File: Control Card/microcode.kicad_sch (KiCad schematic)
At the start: 19 parts, among them U1 CY7C1021D, U100 74LS08, U101 74ACT32, U11 74ACT151, U12 74ACT86, U13 74ACT32, U14 74ACT04, U15 74ACT153, U16 74ACT153, U17 74ACT153, U18 74ACT153, U2 CY7C1021D, U20 74ACT02, U21 74ACT20, U24 74ACT30, U3 CY7C1021D, U44 74ACT11, U53 74ACT04, U61 74ACT32

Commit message: add buffers for the write to the µCODE stuff
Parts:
- removed U100: 74LS08, Package_SO:SOIC-14_3.9x8.7mm_P1.27mm, symbol 74xx:74LS08
- removed U101: 74ACT32, Package_SO:SOIC-14_3.9x8.7mm_P1.27mm, symbol 74xx:74LS32
- added U100: 74LVC1G08, Package_TO_SOT_SMD:SOT-23-5, symbol 74xGxx:74LVC1G08
- added U101: 74LVC1G32, Package_TO_SOT_SMD:SOT-23-5, symbol 74xGxx:74LVC1G32
- added U102: 74LVC1G157, Package_SO:SSOP-8_2.95x2.8mm_P0.65mm, symbol 74xGxx:74LVC2G157
- added U110: 74ACT244, Package_SO:SOIC-20W_7.5x12.8mm_P1.27mm, symbol 74xx:74LS244
- added U111, U112, U113: 74ACT374, Package_SO:SOIC-20W_7.5x12.8mm_P1.27mm, symbol 74xx:74LS374
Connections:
- net GND: now also U100.3 (GND), U101.3 (GND), U102.4 (GND), U102.7 (~G), U110.1 (OEa), U110.10 (GND), U110.19 (OEb), U111.10 (GND), U112.10 (GND), U113.10 (GND)
- net NEXT_0: now also U100.1
- net SUPERVISOR: now also U102.1 (A); no longer U1.27 (A8), U2.27 (A8), U3.27 (A8)
- net VCC: now also U100.5 (VCC), U101.5 (VCC), U102.8 (VCC), U110.20 (VCC), U111.20 (VCC), U112.20 (VCC), U113.20 (VCC)
- net ~FAULT_PENDING~: now also U101.2
- net µCODE_ADDR_SEL_B: now also U101.4
- net µCODE_PAGE0: now also U112.19 (O7), U113.19 (O7)
- net µCODE_PAGE1: now also U112.16 (O6), U113.16 (O6)
- net µCODE_PAGE2: now also U112.15 (O5), U113.15 (O5)
- net µCODE_PAGE3: now also U112.12 (O4), U113.12 (O4)
- net µCODE_PAGE4: now also U112.9 (O3), U113.9 (O3)
- net µCODE_PAGE5: now also U112.6 (O2), U113.6 (O2)
- net µCODE_PAGE6: now also U112.5 (O1), U113.5 (O1)
- net µCODE_WR_ADDR0 renamed µCODE_RW_ADDR0
- net µCODE_RW_ADDR0: now also U111.19 (O7)
- net µCODE_WR_ADDR1 renamed µCODE_RW_ADDR1
- net µCODE_RW_ADDR1: now also U111.16 (O6)
- net µCODE_WR_ADDR2 renamed µCODE_RW_ADDR2
- net µCODE_RW_ADDR2: now also U111.15 (O5)
- net µCODE_WR_ADDR3 renamed µCODE_RW_ADDR3
- net µCODE_RW_ADDR3: now also U111.12 (O4)
- net µCODE_WR_ADDR4 renamed µCODE_RW_ADDR4
- net µCODE_RW_ADDR4: now also U111.9 (O3)
- net µCODE_WR_ADDR5 renamed µCODE_RW_ADDR5
- net µCODE_RW_ADDR5: now also U111.6 (O2)
- net µCODE_WR_ADDR6 renamed µCODE_RW_ADDR6
- net µCODE_RW_ADDR6: now also U111.5 (O1)
- net µCODE_WR_ADDR7 renamed µCODE_RW_ADDR7
- net µCODE_RW_ADDR7: now also U111.2 (O0)
- new net: U100.4, U101.1
- new net DBUS0: U110.17 (I3b)
- new net DBUS1: U110.15 (I2b)
- new net DBUS2: U110.13 (I1b)
- new net DBUS3: U110.11 (I0b)
- new net DBUS4: U110.8 (I3a)
- new net DBUS5: U110.6 (I2a)
- new net DBUS6: U110.4 (I1a)
- new net DBUS7: U110.2 (I0a)
- new net RW_µCODE: U102.6 (~A~/B)
- new net i_DBUS0: U110.3 (O3b), U111.18 (D7), U112.18 (D7), U113.18 (D7)
- new net i_DBUS1: U110.5 (O2b), U111.17 (D6), U112.17 (D6), U113.17 (D6)
- new net i_DBUS2: U110.7 (O1b), U111.14 (D5), U112.14 (D5), U113.14 (D5)
- new net i_DBUS3: U110.9 (O0b), U111.13 (D4), U112.13 (D4), U113.13 (D4)
- new net i_DBUS4: U110.12 (O3a), U111.8 (D3), U112.8 (D3), U113.8 (D3)
- new net i_DBUS5: U110.14 (O2a), U111.7 (D2), U112.7 (D2), U113.7 (D2)
- new net i_DBUS6: U110.16 (O1a), U111.4 (D1), U112.4 (D1), U113.4 (D1)
- new net i_DBUS7: U110.18 (O0a), U111.3 (D0), U112.3 (D0), U113.3 (D0)
- new net ~RW_µCODE~: U100.2
- new net µCODE_RW_SUP: U102.2 (B), U112.2 (O0)
- new net µCODE_SUP: U1.27 (A8), U102.5 (Y), U2.27 (A8), U3.27 (A8)
- no-connect marks 1 -> 2
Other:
- note added: "As currently stands: ~NEXT_0~ ~FAULT_PENDING~ output 0 0 0 (ENCODERx) 1 0 1 (IRx) 0 1 2 (ENCODERx) 1 1 3 (NEXTx) we want: ~RW_µCODE~ ~FAULT_PENDING~ ~NEXT_0~ A B output 0 0 0 0 0 0 (WR_µCODE_R) 0 0 1 1 0 1 (IRx) 0 1 0 0 1 2 (ENCODERx) 0 1 1 1 1 3 (NEXTx) 1 0 0 0 1 2 (ENCODERx) 1 0 1 1 0 1 (IRx) 1 1 0 0 1 2 (ENCODERx) 1 1 1 1 1 3 (NEXTx) B = ~FAULT_PENDING~ or ( ~RW_µCODE~ and NEXT_0 )"
- note added: "Buffer"
- note added: "Execute"
- note added: "Read/Write"
- note added: "Selects supervisor bit between the faults generator and the µCODE_RW registers"
- note removed: "As currently stands: ~NEXT_0~ ~FAULT_PENDING~ output 0 0 0 (ENCODERx) 1 0 1 (IRx) 0 1 2 (ENCODERx) 1 1 3 (NEXTx) we want: ~WR_µCODE~ ~FAULT_PENDING~ ~NEXT_0~ A B output 0 0 0 0 0 0 (WR_µCODE_R) 0 0 1 1 0 1 (IRx) 0 1 0 0 1 2 (ENCODERx) 0 1 1 1 1 3 (NEXTx) 1 0 0 0 1 2 (ENCODERx) 1 0 1 1 0 1 (IRx) 1 1 0 0 1 2 (ENCODERx) 1 1 1 1 1 3 (NEXTx) B = ~FAULT_PENDING~ or ( ~WR_µCODE~ and NEXT_0 )"

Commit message: add the µcode output registers
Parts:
- added U10, U5, U6, U7, U8, U9: 74ACT273, Package_SO:SOIC-20W_7.5x12.8mm_P1.27mm, symbol 74xx:74LS273
- U102: value 74LVC1G157 -> 74LVC2G157
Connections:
- net ALUOP0: now also U10.6 (Q2); no longer U3.31 (D10)
- net ALUOP1: now also U10.5 (Q1); no longer U3.30 (D9)
- net ALUOP_SZ: now also U10.2 (Q0); no longer U3.29 (D8)
- net CODE_PTB: now also U10.19 (Q7); no longer U3.38 (D15)
- net EL0: now also U9.9 (Q3); no longer U3.10 (D3)
- net EL1: now also U9.6 (Q2); no longer U3.9 (D2)
- net EL2: now also U9.5 (Q1); no longer U3.8 (D1)
- net EL3: now also U9.2 (Q0); no longer U3.7 (D0)
- net ER0: now also U9.15 (Q5); no longer U3.14 (D5)
- net ER1: now also U9.12 (Q4); no longer U3.13 (D4)
- net E_MDR_HI: now also U8.2 (Q0); no longer U2.29 (D8)
- net E_MDR_LO: now also U7.19 (Q7); no longer U2.16 (D7)
- net GND: now also U10.10 (GND), U5.10 (GND), U6.10 (GND), U7.10 (GND), U8.10 (GND), U9.10 (GND)
- net LATCH0: now also U7.9 (Q3); no longer U2.10 (D3)
- net LATCH1: now also U7.6 (Q2); no longer U2.9 (D2)
- net LATCH2: now also U7.5 (Q1); no longer U2.8 (D1)
- net LATCH3: now also U7.2 (Q0); no longer U2.7 (D0)
- net LATCH_SZ: now also U10.12 (Q4); no longer U3.35 (D12)
- net MISC0: now also U8.19 (Q7); no longer U2.38 (D15)
- net MISC1: now also U8.16 (Q6); no longer U2.37 (D14)
- net MISC2: now also U8.15 (Q5); no longer U2.36 (D13)
- net MISC3: now also U8.12 (Q4); no longer U2.35 (D12)
- net NEGATE_BR: now also U10.15 (Q5); no longer U3.36 (D13)
- net NEXT0: now also U6.19 (Q7); no longer U1.16 (D7)
- net NEXT1: now also U6.16 (Q6); no longer U1.15 (D6)
- net NEXT2: now also U6.15 (Q5); no longer U1.14 (D5)
- net NEXT3: now also U6.12 (Q4); no longer U1.13 (D4)
- net NEXT4: now also U6.9 (Q3); no longer U1.10 (D3)
- net NEXT5: now also U6.6 (Q2); no longer U1.9 (D2)
- net NEXT6: now also U6.5 (Q1); no longer U1.8 (D1)
- net NEXT7: now also U6.2 (Q0); no longer U1.7 (D0)
- net PRIV: now also U8.5 (Q1); no longer U2.30 (D9)
- net RIMMVAL0: now also U9.19 (Q7); no longer U3.16 (D7)
- net RIMMVAL1: now also U9.16 (Q6); no longer U3.15 (D6)
- net RUSER_PTB: now also U10.16 (Q6); no longer U3.37 (D14)
- net USE_CARRY: now also U10.9 (Q3); no longer U3.32 (D11)
- net VCC: now also U10.20 (VCC), U5.20 (VCC), U6.20 (VCC), U7.20 (VCC), U8.20 (VCC), U9.20 (VCC)
- net XL_MAR: now also U7.12 (Q4); no longer U2.13 (D4)
- net XL_MDR_HI: now also U7.16 (Q6); no longer U2.15 (D6)
- net XL_MDR_LO: now also U7.15 (Q5); no longer U2.14 (D5)
- net XL_MODE: now also U8.6 (Q2); no longer U2.31 (D10)
- net XL_PAGING: now also U8.9 (Q3); no longer U2.32 (D11)
- new net CLKM: U10.11 (Cp), U5.11 (Cp), U6.11 (Cp), U7.11 (Cp), U8.11 (Cp), U9.11 (Cp)
- new net _RESET: U10.1 (~Mr), U5.1 (~Mr), U6.1 (~Mr), U7.1 (~Mr), U8.1 (~Mr), U9.1 (~Mr)
- new net io_ALUOP0: U10.7 (D2), U3.31 (D10)
- new net io_ALUOP1: U10.4 (D1), U3.30 (D9)
- new net io_ALUOP_SZ: U10.3 (D0), U3.29 (D8)
- new net io_CODE_PTB: U10.18 (D7), U3.38 (D15)
- new net io_EL0: U3.10 (D3), U9.8 (D3)
- new net io_EL1: U3.9 (D2), U9.7 (D2)
- new net io_EL2: U3.8 (D1), U9.4 (D1)
- new net io_EL3: U3.7 (D0), U9.3 (D0)
- new net io_ER0: U3.14 (D5), U9.14 (D5)
- new net io_ER1: U3.13 (D4), U9.13 (D4)
- new net io_E_MDR_HI: U2.29 (D8), U8.3 (D0)
- new net io_E_MDR_LO: U2.16 (D7), U7.18 (D7)
- new net io_LATCH0: U2.10 (D3), U7.8 (D3)
- new net io_LATCH1: U2.9 (D2), U7.7 (D2)
- new net io_LATCH2: U2.8 (D1), U7.4 (D1)
- new net io_LATCH3: U2.7 (D0), U7.3 (D0)
- new net io_LATCH_SZ: U10.13 (D4), U3.35 (D12)
- new net io_MISC0: U2.38 (D15), U8.18 (D7)
- new net io_MISC1: U2.37 (D14), U8.17 (D6)
- new net io_MISC2: U2.36 (D13), U8.14 (D5)
- new net io_MISC3: U2.35 (D12), U8.13 (D4)
- new net io_NEGATE_BR: U10.14 (D5), U3.36 (D13)
- new net io_NEXT0: U1.16 (D7), U6.18 (D7)
- new net io_NEXT1: U1.15 (D6), U6.17 (D6)
- new net io_NEXT2: U1.14 (D5), U6.14 (D5)
- new net io_NEXT3: U1.13 (D4), U6.13 (D4)
- new net io_NEXT4: U1.10 (D3), U6.8 (D3)
- new net io_NEXT5: U1.9 (D2), U6.7 (D2)
- new net io_NEXT6: U1.8 (D1), U6.4 (D1)
- new net io_NEXT7: U1.7 (D0), U6.3 (D0)
- new net io_PRIV: U2.30 (D9), U8.4 (D1)
- new net io_RIMMVAL0: U3.16 (D7), U9.18 (D7)
- new net io_RIMMVAL1: U3.15 (D6), U9.17 (D6)
- new net io_RUSER_PTB: U10.17 (D6), U3.37 (D14)
- new net io_USE_CARRY: U10.8 (D3), U3.32 (D11)
- new net io_XL_MAR: U2.13 (D4), U7.13 (D4)
- new net io_XL_MDR_HI: U2.15 (D6), U7.17 (D6)
- new net io_XL_MDR_LO: U2.14 (D5), U7.14 (D5)
- new net io_XL_MODE: U2.31 (D10), U8.7 (D2)
- new net io_XL_PAGING: U2.32 (D11), U8.8 (D3)

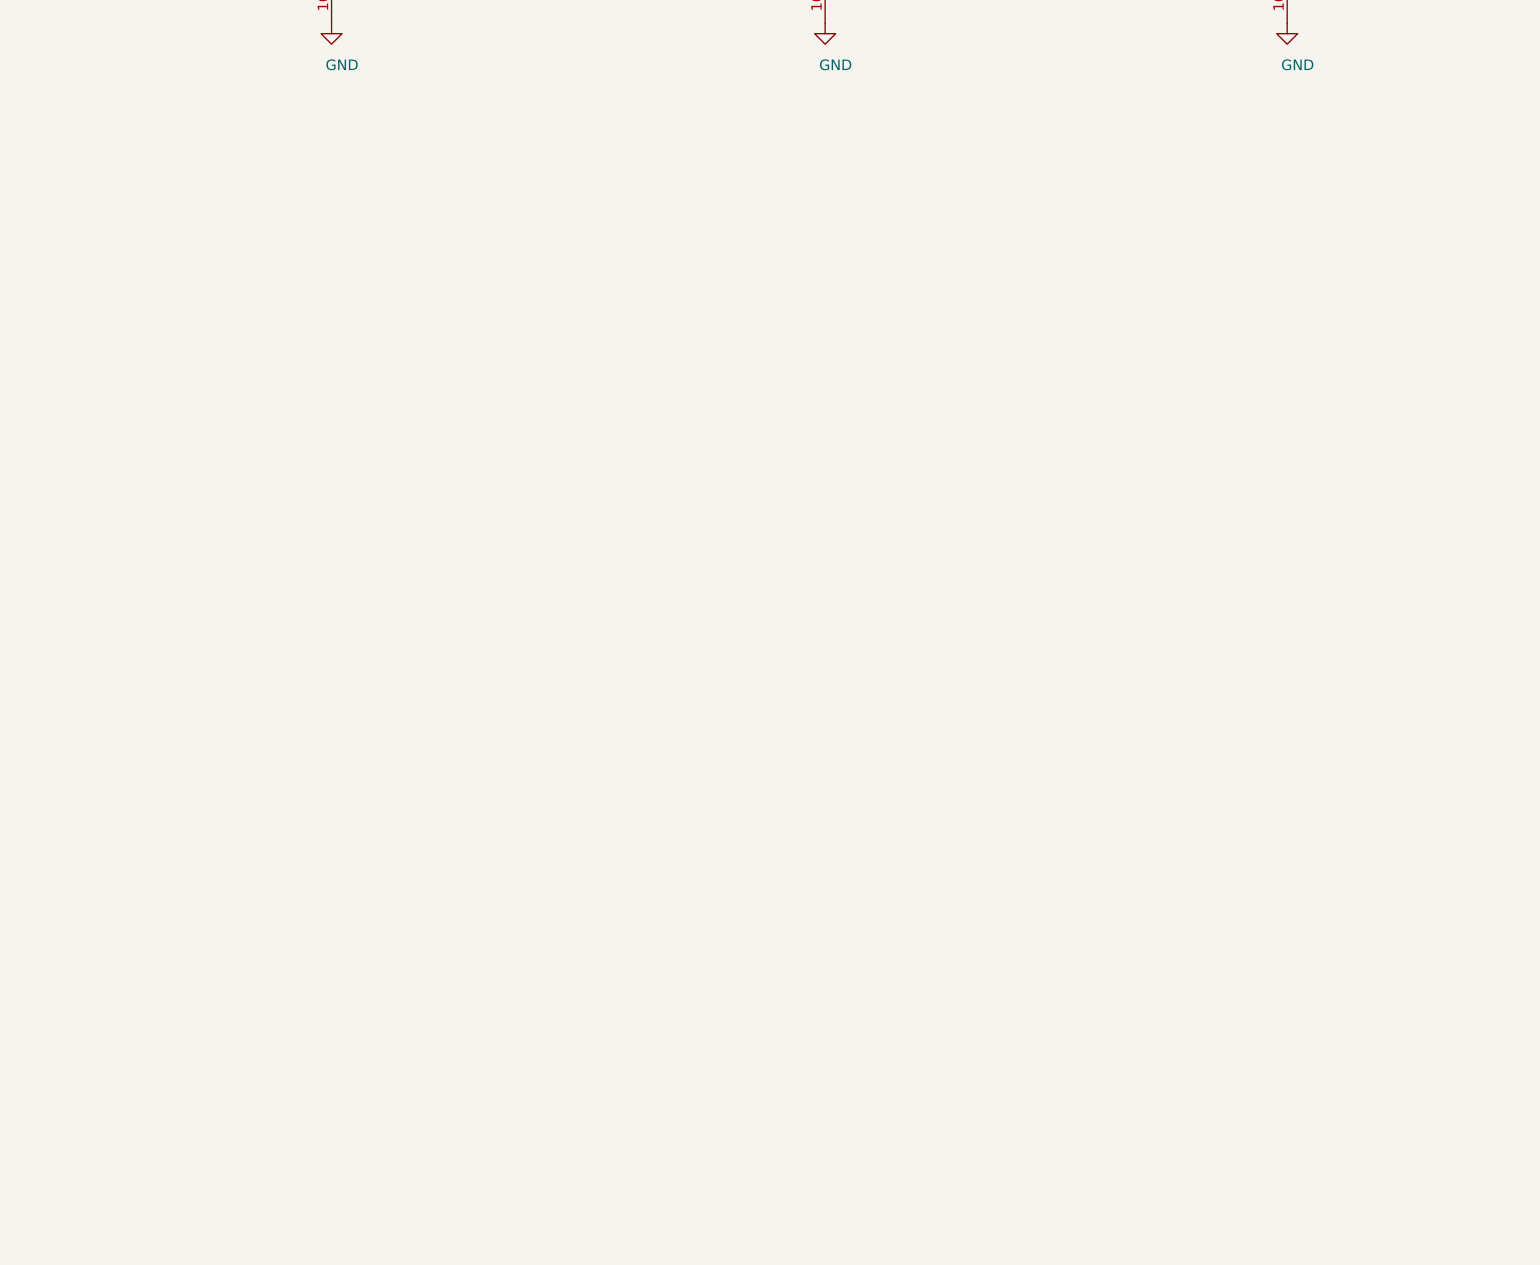
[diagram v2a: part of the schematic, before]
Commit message: add the µcode data write registers
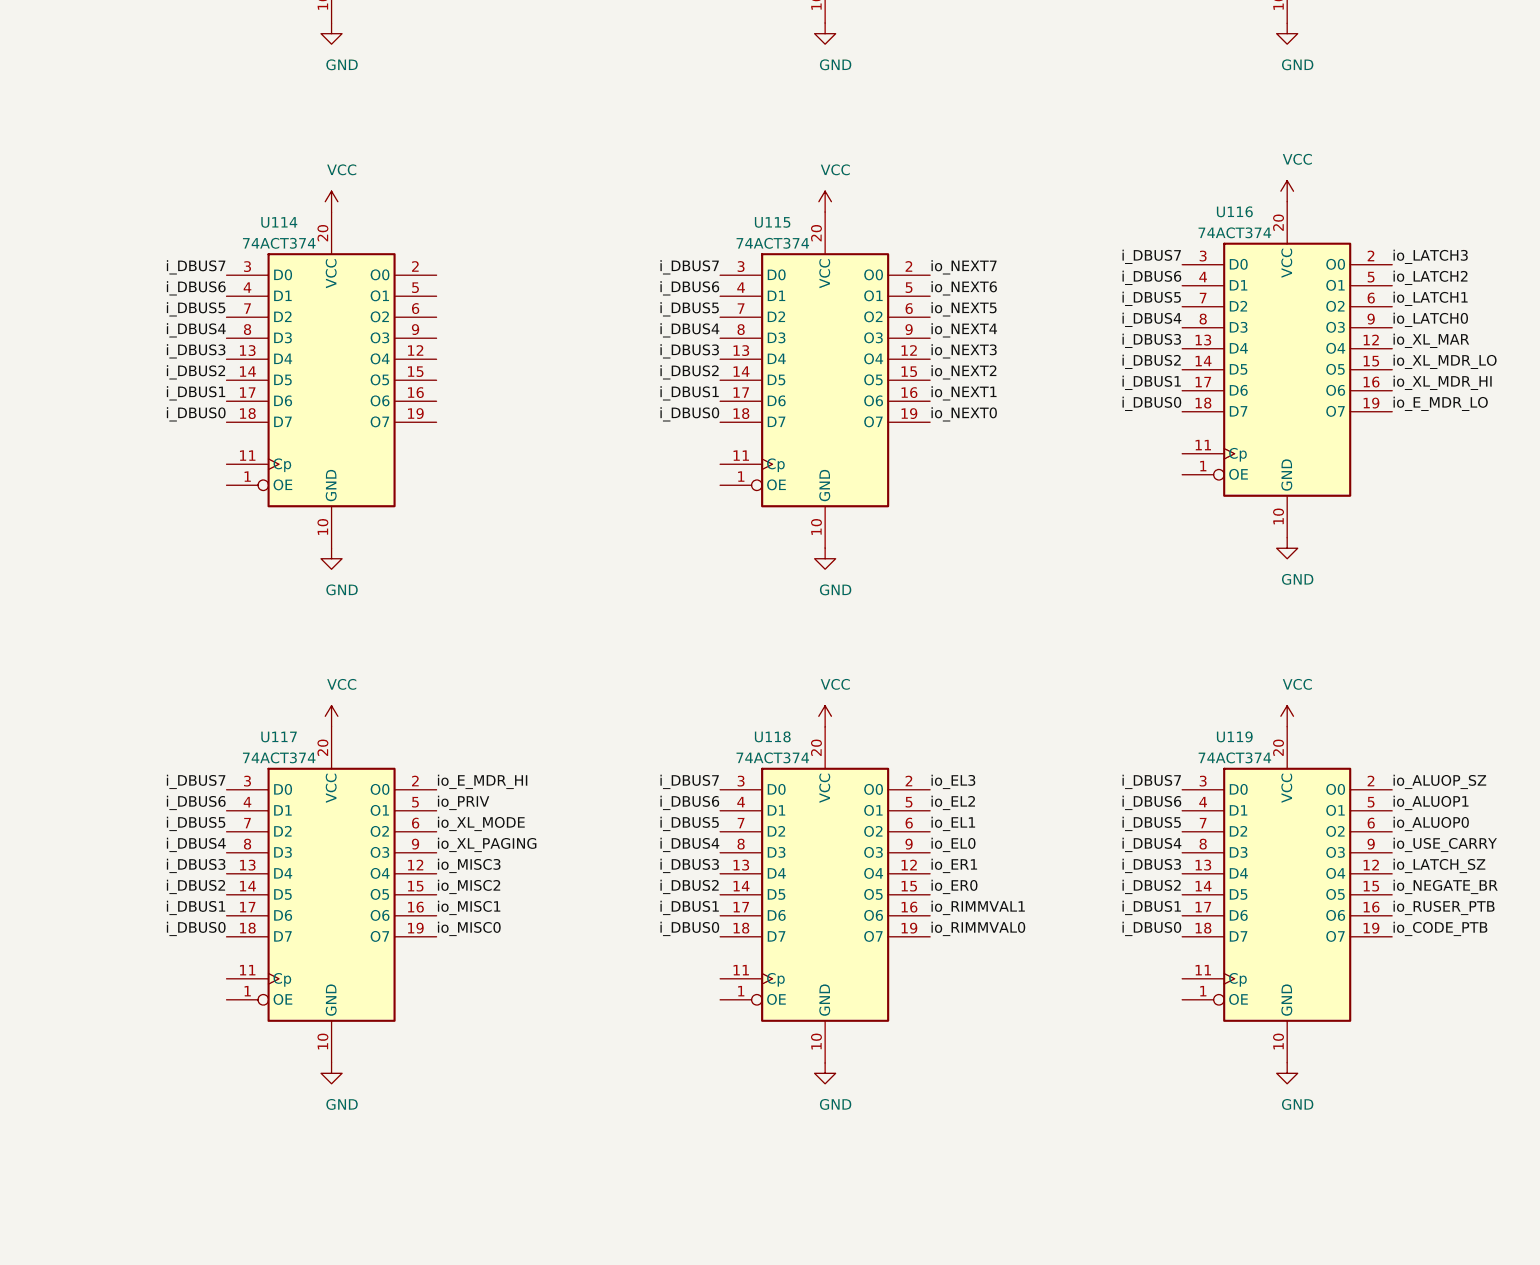
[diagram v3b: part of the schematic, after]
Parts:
- added U114, U115, U116, U117, U118, U119: 74ACT374, Package_SO:SOIC-20W_7.5x12.8mm_P1.27mm, symbol 74xx:74LS374
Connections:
- net GND: now also U114.10 (GND), U115.10 (GND), U116.10 (GND), U117.10 (GND), U118.10 (GND), U119.10 (GND)
- net VCC: now also U114.20 (VCC), U115.20 (VCC), U116.20 (VCC), U117.20 (VCC), U118.20 (VCC), U119.20 (VCC)
- net i_DBUS0: now also U114.18 (D7), U115.18 (D7), U116.18 (D7), U117.18 (D7), U118.18 (D7), U119.18 (D7)
- net i_DBUS1: now also U114.17 (D6), U115.17 (D6), U116.17 (D6), U117.17 (D6), U118.17 (D6), U119.17 (D6)
- net i_DBUS2: now also U114.14 (D5), U115.14 (D5), U116.14 (D5), U117.14 (D5), U118.14 (D5), U119.14 (D5)
- net i_DBUS3: now also U114.13 (D4), U115.13 (D4), U116.13 (D4), U117.13 (D4), U118.13 (D4), U119.13 (D4)
- net i_DBUS4: now also U114.8 (D3), U115.8 (D3), U116.8 (D3), U117.8 (D3), U118.8 (D3), U119.8 (D3)
- net i_DBUS5: now also U114.7 (D2), U115.7 (D2), U116.7 (D2), U117.7 (D2), U118.7 (D2), U119.7 (D2)
- net i_DBUS6: now also U114.4 (D1), U115.4 (D1), U116.4 (D1), U117.4 (D1), U118.4 (D1), U119.4 (D1)
- net i_DBUS7: now also U114.3 (D0), U115.3 (D0), U116.3 (D0), U117.3 (D0), U118.3 (D0), U119.3 (D0)
- net io_ALUOP0: now also U119.6 (O2)
- net io_ALUOP1: now also U119.5 (O1)
- net io_ALUOP_SZ: now also U119.2 (O0)
- net io_CODE_PTB: now also U119.19 (O7)
- net io_EL0: now also U118.9 (O3)
- net io_EL1: now also U118.6 (O2)
- net io_EL2: now also U118.5 (O1)
- net io_EL3: now also U118.2 (O0)
- net io_ER0: now also U118.15 (O5)
- net io_ER1: now also U118.12 (O4)
- net io_E_MDR_HI: now also U117.2 (O0)
- net io_E_MDR_LO: now also U116.19 (O7)
- net io_LATCH0: now also U116.9 (O3)
- net io_LATCH1: now also U116.6 (O2)
- net io_LATCH2: now also U116.5 (O1)
- net io_LATCH3: now also U116.2 (O0)
- net io_LATCH_SZ: now also U119.12 (O4)
- net io_MISC0: now also U117.19 (O7)
- net io_MISC1: now also U117.16 (O6)
- net io_MISC2: now also U117.15 (O5)
- net io_MISC3: now also U117.12 (O4)
- net io_NEGATE_BR: now also U119.15 (O5)
- net io_NEXT0: now also U115.19 (O7)
- net io_NEXT1: now also U115.16 (O6)
- net io_NEXT2: now also U115.15 (O5)
- net io_NEXT3: now also U115.12 (O4)
- net io_NEXT4: now also U115.9 (O3)
- net io_NEXT5: now also U115.6 (O2)
- net io_NEXT6: now also U115.5 (O1)
- net io_NEXT7: now also U115.2 (O0)
- net io_PRIV: now also U117.5 (O1)
- net io_RIMMVAL0: now also U118.19 (O7)
- net io_RIMMVAL1: now also U118.16 (O6)
- net io_RUSER_PTB: now also U119.16 (O6)
- net io_USE_CARRY: now also U119.9 (O3)
- net io_XL_MAR: now also U116.12 (O4)
- net io_XL_MDR_HI: now also U116.16 (O6)
- net io_XL_MDR_LO: now also U116.15 (O5)
- net io_XL_MODE: now also U117.6 (O2)
- net io_XL_PAGING: now also U117.9 (O3)

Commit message: connect the enable lines for the µcode rams
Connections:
- net GND: now also U1.6 (~CE~), U2.6 (~CE~), U3.6 (~CE~)
- net ~µCODE_WR~: now reaches U3.17 (~WE~)
- net ~µCODE_WR~: now also U1.17 (~WE~), U2.17 (~WE~)
- net ~µCODE_RD~: now reaches U3.39 (~BLE~)
- net ~µCODE_RD~: now also U1.39 (~BLE~), U1.40 (~BHE~), U1.41 (~OE~), U2.39 (~BLE~), U2.40 (~BHE~), U2.41 (~OE~), U3.40 (~BHE~), U3.41 (~OE~)
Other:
- note added: "Necessary for fanout"
- note removed: "Buffer"

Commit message: add what I think are the necessary lines to control writing to the µcode store
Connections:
- net io_µCODE_REGISTERS2: now reaches U1.29 (D8)
- net io_µCODE_REGISTERS2: now also U114.2 (O0), U5.3 (D0)
- net io_µCODE_REGISTERS1: now reaches U1.30 (D9)
- net io_µCODE_REGISTERS1: now also U114.5 (O1), U5.4 (D1)
- net io_µCODE_REGISTERS0: now reaches U1.31 (D10)
- net io_µCODE_REGISTERS0: now also U114.6 (O2), U5.7 (D2)
- net io_µCODE_L_REGISTERS: now reaches U1.32 (D11)
- net io_µCODE_L_REGISTERS: now also U114.9 (O3), U5.8 (D3)
- net io_µCODE_WR_PRIME: now reaches U1.35 (D12)
- net io_µCODE_WR_PRIME: now also U114.12 (O4), U5.13 (D4)
- net io_µCODE_L_RUN_PAGE: now reaches U1.36 (D13)
- net io_µCODE_L_RUN_PAGE: now also U114.15 (O5), U5.14 (D5)
- net µCODE_WR_PRIME: now reaches U5.12 (Q4)
- net µCODE_L_RUN_PAGE: now reaches U5.15 (Q5)
- net µCODE_REGISTERS2: now reaches U5.2 (Q0)
- net µCODE_REGISTERS1: now reaches U5.5 (Q1)
- net µCODE_REGISTERS0: now reaches U5.6 (Q2)
- net µCODE_L_REGISTERS: now reaches U5.9 (Q3)
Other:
- moved on the sheet: U1, U5
